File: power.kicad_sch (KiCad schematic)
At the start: 35 parts, among them J1 Battery 1, J7 Battery 2, J8 USB, U1 AMS1117-3.3, U5 TPS62933, U6 TPS62933

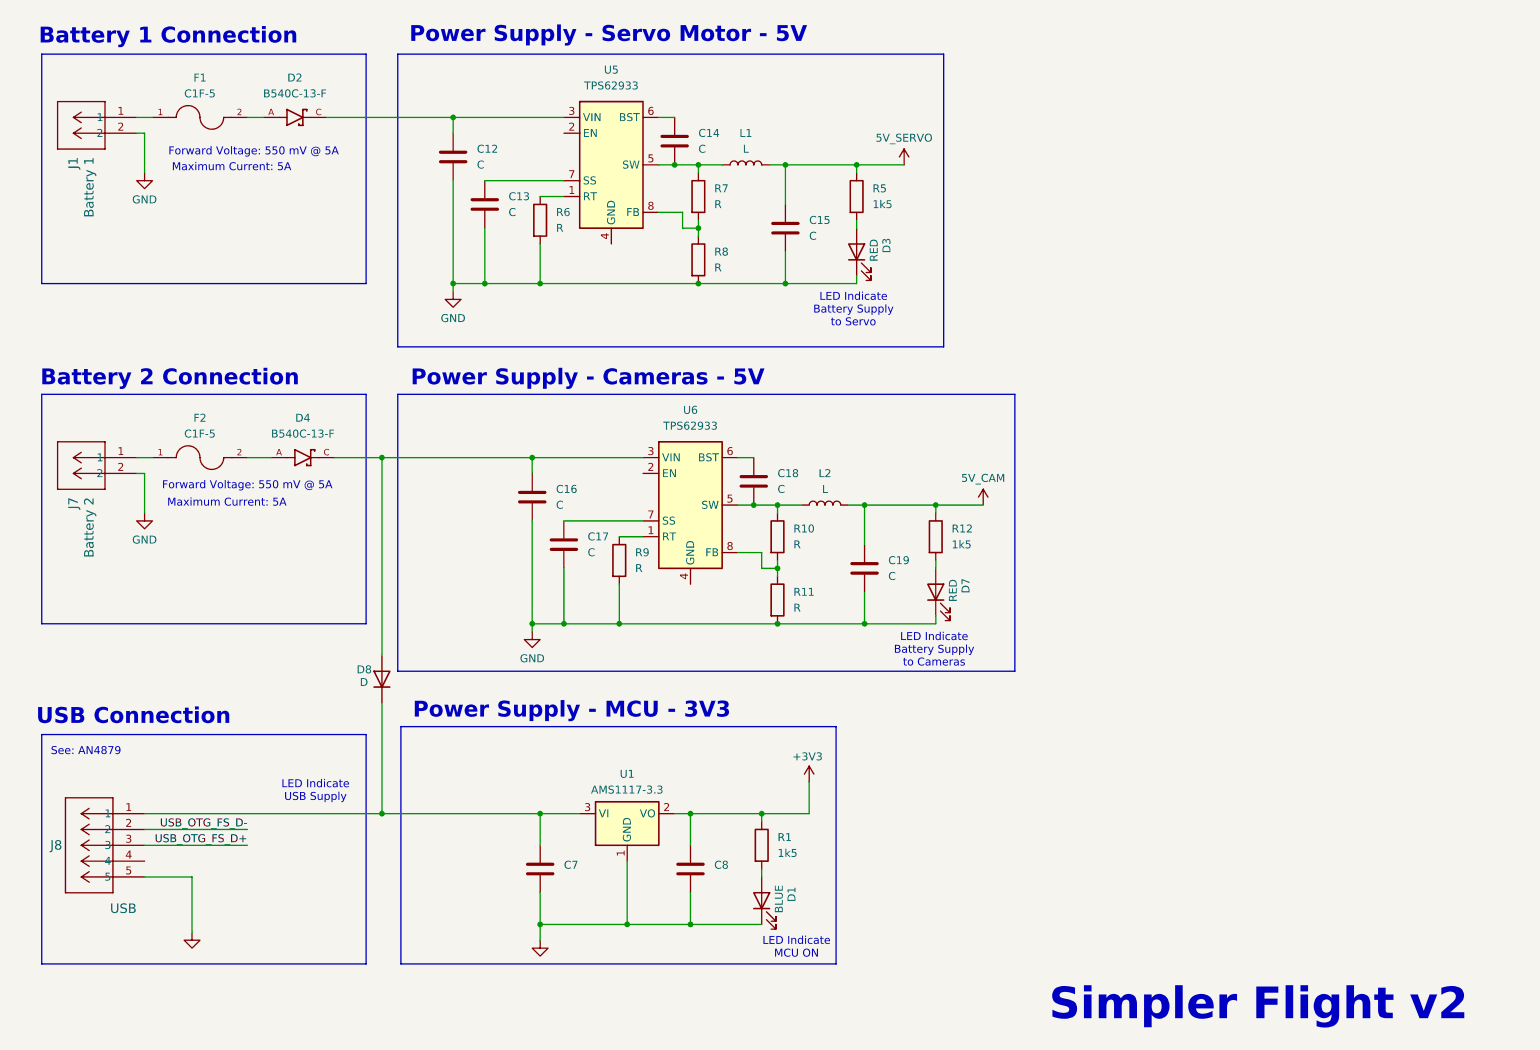
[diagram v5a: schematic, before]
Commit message: Update schematic, pending power sims, updated README
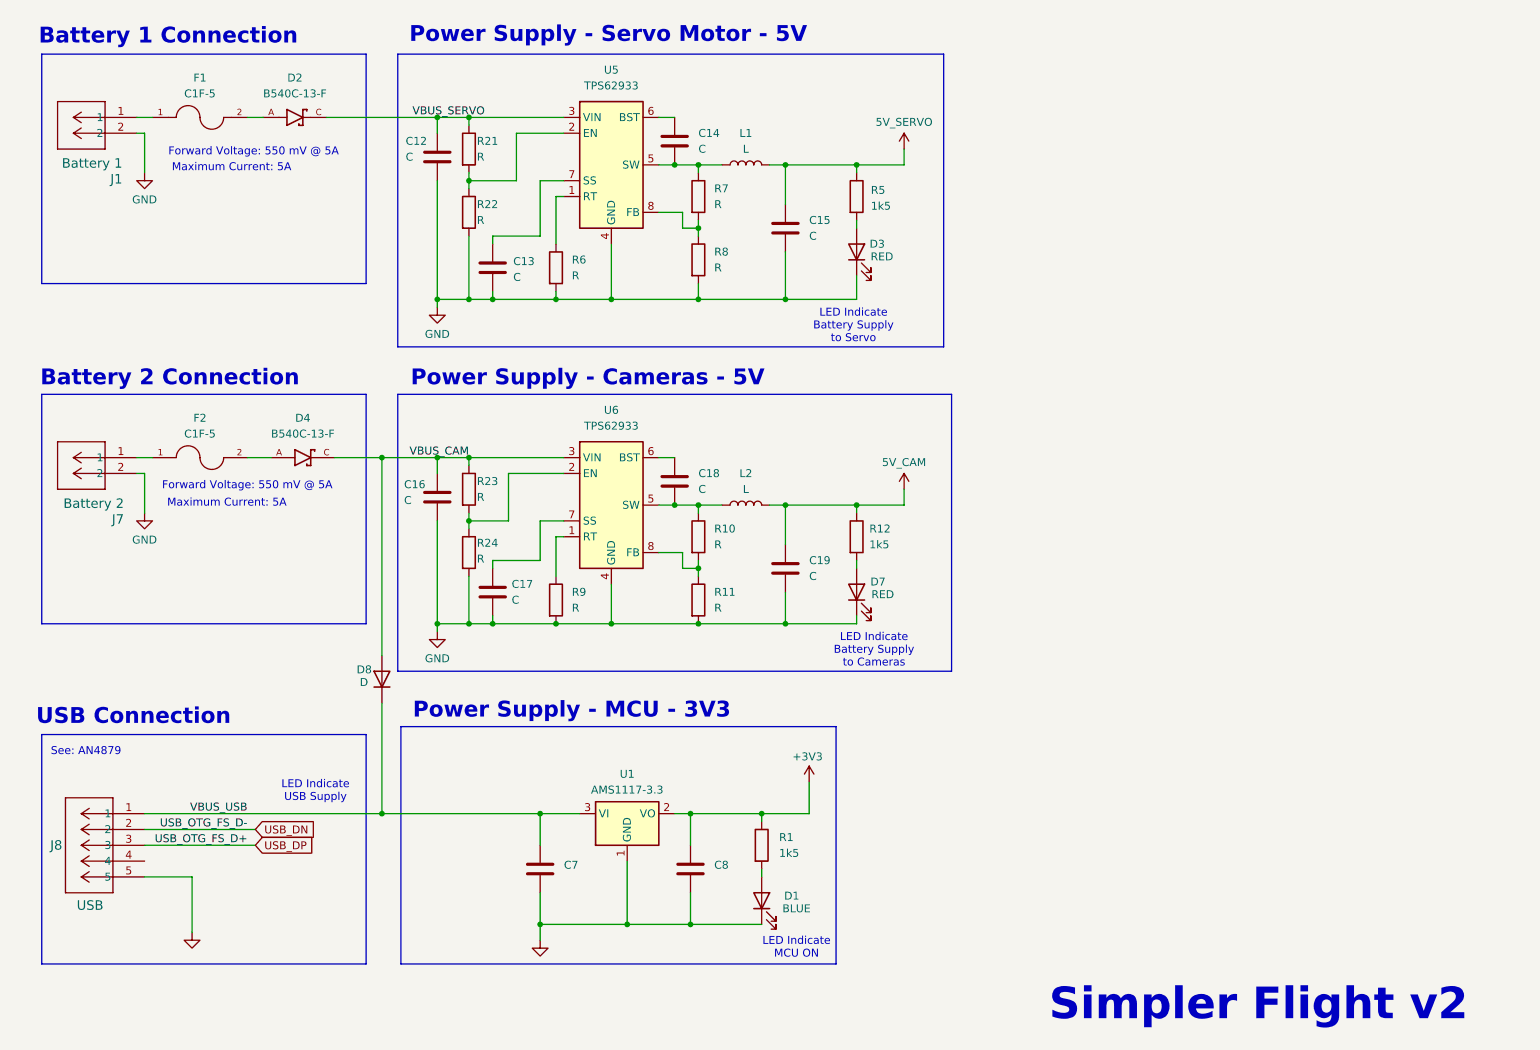
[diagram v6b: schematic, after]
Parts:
- added R21, R22, R23, R24: R, Resistor_SMD:R_0805_2012Metric_Pad1.20x1.40mm_HandSolder, symbol Device:R
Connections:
- net GND: now also U5.4 (GND), U6.4 (GND), R22.2, R24.2
- net VBUS_CAM: now reaches C16.1, D4.C, D8.2 (A), U6.3 (VIN)
- net VBUS_CAM: now also R23.1
- net VBUS_SERVO: now reaches C12.1, D2.C, U5.3 (VIN)
- net VBUS_SERVO: now also R21.1
- net VBUS_USB: now reaches C7.1, D8.1 (K), J8.1, U1.3 (VI)
- net at U5.2 (EN): now also R21.2, R22.1
- net at U6.2 (EN): now also R23.2, R24.1
- net USB_OTG_FS_D+ renamed USB_DP
- net USB_OTG_FS_D- renamed USB_DN
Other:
- moved on the sheet: C12, C13, C16, C17, C18, C19, D7, L2, R10, R11, R12, R6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
